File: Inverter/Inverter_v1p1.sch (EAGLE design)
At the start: 39 parts, among them J2 2-pos, J3 2-pos, Q27 RJH60F7DPQ-A0T0, Q28 RJH60F7DPQ-A0T0, Q29 STGW30H60DFB, Q30 STGW30H60DFB, Q31 STGW30H60DFB, Q32 STGW30H60DFB

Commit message: Updated Schematic
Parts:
- D38: value GF1D-E3 -> ZJF_638
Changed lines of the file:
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@@
 <part name="R142" library="3D_MIG_Controller" deviceset="R_0805" device=""/>
 <part name="D35" library="3D_MIG_Controller" deviceset="GF1D-E3" device=""/>
-<part name="D38" library="3D_MIG_Controller" deviceset="GF1D-E3" device=""/>
+<part name="D38" library="3D_MIG_Controller" deviceset="GF1D-E3" device="" value="ZJF_638"/>
 <part name="D41" library="3D_MIG_Controller" deviceset="GF1D-E3" device=""/>
 <part name="D42" library="3D_MIG_Controller" deviceset="GF1D-E3" device=""/>

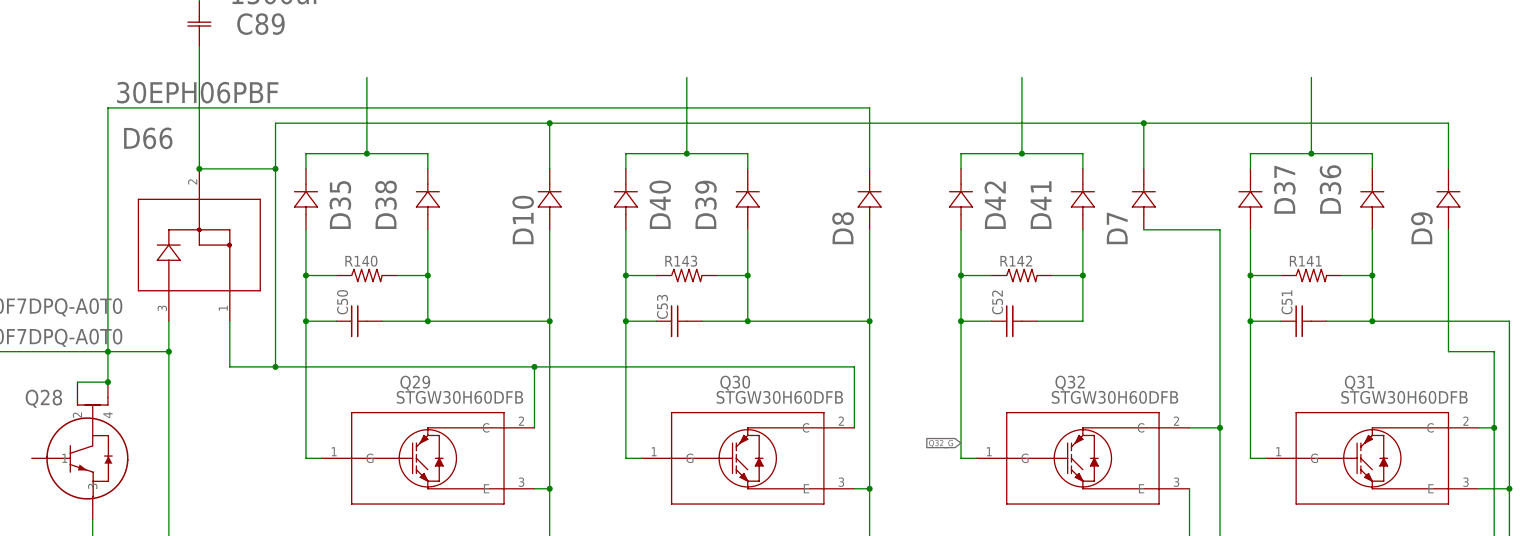
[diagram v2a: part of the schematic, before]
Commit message: Updated to include correct diodes on power side of circuit.
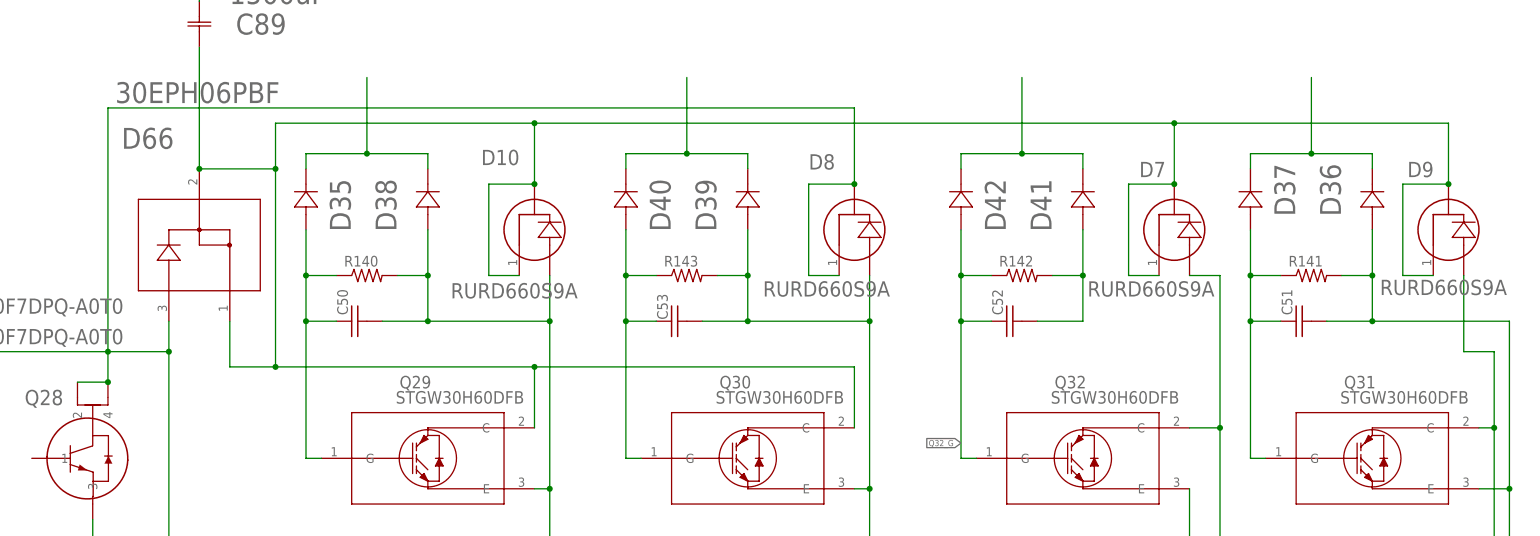
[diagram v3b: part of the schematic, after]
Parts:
- D10, D7, D8, D9: value GF1D-E3 -> RURD660S9A; device 3D_MIG_Controller:GF1D-E3 -> 3D_MIG_Controller:RURD660S9A
- D35, D36, D37, D39, D40, D41, D42: value GF1D-E3 -> SMAZ18-13-FSMA_DIO-M; device 3D_MIG_Controller:GF1D-E3 -> 3D_MIG_Controller:SMAZ18-13-FSMA_DIO-M
- D38: device 3D_MIG_Controller:GF1D-E3 -> 3D_MIG_Controller:SMAZ18-13-FSMA_DIO-M
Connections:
- net D66_1: now also D10.C1, D10.C2, D7.C1, D7.C2, D9.C1, D9.C2; no longer D10.1, D7.1, D9.1
- net RC20_RED: now also D10.A; no longer D10.2
- net RC21_BLK: now also D9.A; no longer D9.2
- net RC22_GRN: now also D7.A; no longer D7.2
- net RC23_YEL: now also D8.A; no longer D8.2
- net RC25_ORG: now also D8.C1, D8.C2; no longer D8.1
